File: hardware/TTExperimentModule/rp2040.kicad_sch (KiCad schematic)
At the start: 24 parts, among them J6 Conn_01x02, U5 RP2040, U6 W25Q32JVSS, Y1 12.0MHz

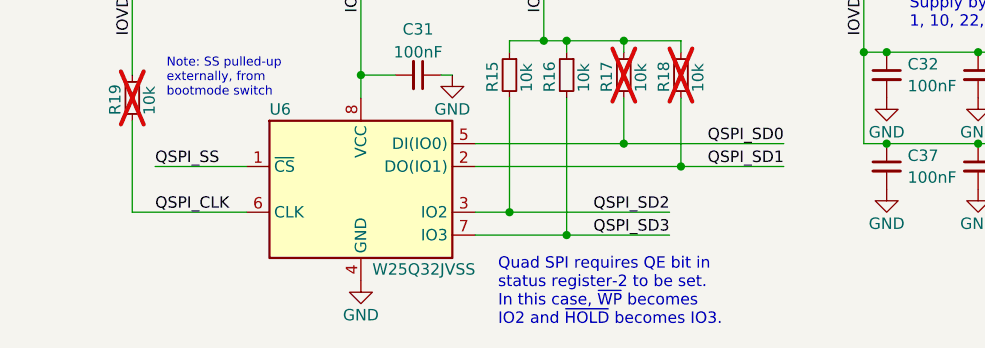
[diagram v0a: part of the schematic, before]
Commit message: reduced-height flash (dual footprint), layout rework, markings
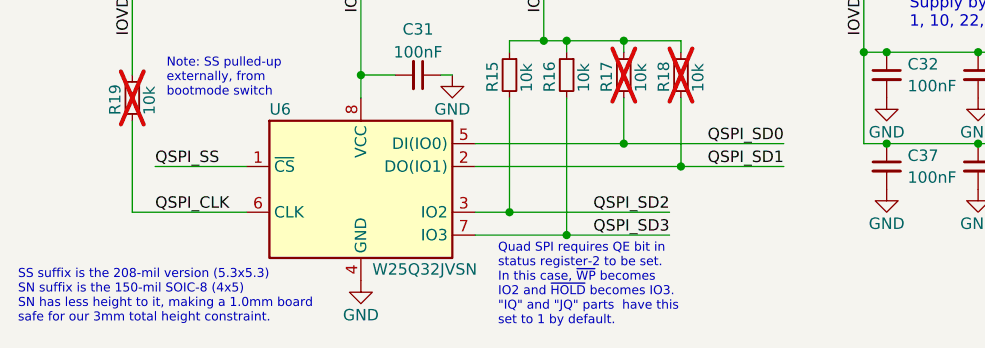
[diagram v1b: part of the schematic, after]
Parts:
- U6: value W25Q32JVSS -> W25Q32JVSN; footprint Package_SO:SOIC-8_5.3x5.3mm_P1.27mm -> Package_SO:SOIC-8_3.9x4.9mm_P1.27mm; DigikeyPN W25Q32JVSSIQ-ND -> 256-W25Q32JVSNIQTRCT-ND; LCSC C82344 -> C5355146; MPN W25Q32JVSSIQ -> W25Q32JVSNIQ TR
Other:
- note added: "Quad SPI requires QE bit in status register-2 to be set. In this case, ~{WP} becomes IO2 and ~{HOLD} becomes IO3. "IQ" and "JQ" parts have this set to 1 by default."
- note added: "SS suffix is the 208-mil version (5.3x5.3) SN suffix is the 150-mil SOIC-8 (4x5) SN has less height to it, making a 1.0mm board safe for our 3mm total height constraint."
- note removed: "Quad SPI requires QE bit in status register-2 to be set. In this case, ~{WP} becomes IO2 and ~{HOLD} becomes IO3."
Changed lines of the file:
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@@
 		)
 	)
-	(text "Quad SPI requires QE bit in \nstatus register-2 to be set.\nIn this case, ~{WP} becomes \nIO2 and ~{HOLD} becomes IO3."
+	(text "Quad SPI requires QE bit in \nstatus register-2 to be set.\nIn this case, ~{WP} becomes \nIO2 and ~{HOLD} becomes IO3.\n\"IQ\" and \"JQ\" parts  have this\nset to 1 by default."
 		(exclude_from_sim no)
 		(at 66.04 195.58 0)
 		(effects
 			(font
-				(size 1.27 1.27)
+				(size 1 1)
 			)
 			(justify left bottom)
 		)
 	)
+	(text "SS suffix is the 208-mil version (5.3x5.3)\nSN suffix is the 150-mil SOIC-8 (4x5)\nSN has less height to it, making a 1.0mm board\nsafe for our 3mm total height constraint."
+		(exclude_from_sim no)
+		(at 12.7 192.278 0)
+		(effects
+			(font
+				(size 1 1)
+			)
+			(justify left)
+		)
+	)
 	(text "Factory test\nmode: GND"
 		(exclude_from_sim no)
@@
 			"NS0wMy0yOVQyMDoxNDo0My41NjEyODNaIiBjb3VudD0iMSIvPgogICAgICAgIDwvYm9va21hcms6"
 			"YXBwbGljYXRpb25zPgogICAgICA8L21ldGFkYXRhPgogICAgPC9pbmZvPgogIDwvYm9va21hcms+"
-			"CiAgPGJvb2ttYXJrIGhyZWY9ImZpbGU6Lw=="
+			"CiAgPGJvb2ttYXJrIGhyZWY9ImZpbGU6LwBRAAAATgAAAGcAAABXAAAAawAAADUAAABlAAAAOAAA"
+			"ADEAAAB0AAAAOAAAADYAAABJAAAAUgAAAFgAAAAvAAAAVQAAAFgAAAB4AAAANgAAAHEAAABvAAAA"
+			"NgAAAEIAAAB0AAAALwAAAEcAAAAyAAAAbAAAAEIAAAAvAAAAZwAAAE0AAABPAAAARQAAAEMAAABZ"
+			"AAAANgAAADYAAAArAAAAZgAAAFEAAAA0AAAAMgAAAGkAAAB6AAAAQgAAADkAAABMAAAAbAAAAGMA"
+			"AABRAAAAMwAAADIAAAB1AAAALwAAAFkAAAB5AAAAdgAAAGYAAAA1AAAAagAAAHQAAAA4AAAAUAAA"
+			"AG8AAABWAAAARAAAAGEAAABiAAAAeAAAAGMAAABOAAAAKwAAAHgAAAAxAAAAaAAAAFUAAAB2AAAA"
+			"bAAAAE0AAABzAAAAQQAAADYAAABJAAAAMgAAAGEAAABHAAAAeQAAAFUAAABNAAAAQwAAAGIAAABB"
+			"AAAAMwAAADYAAABxAAAAcgAAAGQAAABLAAAAYwAAADkAAAByAAAANgAAAFoAAABmAAAAVwAAAGwA"
+			"AAA3AAAAWgAAAEUAAABSAAAALwAAACsAAABTAAAANwAAAFIAAABVAAAAeQAAAGYAAAAxAAAAUwAA"
+			"AFAAAAB1AAAAcwAAAEMAAABUAAAAegAAAE0AAAAxAAAAUAAAAHUAAABzAAAAMQAAAGYAAAB1AAAA"
+			"TQAAAHEAAAAxAAAATQAAAFAAAABsAAAAVwAAAFUAAAA2AAAAZgAAAC8AAABZAAAASgAAAHMAAAA3"
+			"AAAATwAAAHcAAAAxAAAAdAAAAHIAAABTAAAARQAAAHQAAABQAAAAbgAAAGgAAABWAAAAVAAAAG8A"
+			"AABHAAAAeAAAAHgAAAA4AAAAUwAAAGgAAABIAAAAQwAAAE4AAABIAAAAWAAAAHoAAABmAAAAMAAA"
+			"AFUAAABhAAAANQAAAEUAAAA1AAAAZgAAADgAAAAxAAAAagAAAFMAAABNAAAANQAAAHAAAABsAAAA"
+			"dAAAAG0AAABNAAAAagAAAGoAAABPAAAAUQAAAFcAAABzAAAAVwAAAGUAAABGAAAAcgAAAG8AAAA4"
+			"AAAAKwAAAHkAAABHAAAARAAAADIAAABiAAAAaAAAAFIAAABOAAAATwAAAHQAAAA1AAAARQAAAEsA"
+			"AAAzAAAAQgAAAGYAAAA5AAAAeQAAAEgAAABxAAAAaAAAAHYAAABiAAAAQgAAAGUAAAB3AAAAZQAA"
+			"AE4AAABGAAAAbwAAAGIAAABvAAAAdAAAAEMAAAB2AAAAVAAAAHQAAABKAAAANAAAAFYAAABBAAAA"
+			"egAAAHMAAABsAAAAdQAAAFcAAABrAAAASA=="
 		)
 	)
@@
 			)
 		)
-		(property "Value" "W25Q32JVSS"
+		(property "Value" "W25Q32JVSN"
 			(at 52.07 189.23 0)
 			(effects
@@
 			)
 		)
-		(property "Footprint" "Package_SO:SOIC-8_5.3x5.3mm_P1.27mm"
+		(property "Footprint" "Package_SO:SOIC-8_3.9x4.9mm_P1.27mm"
 			(at 50.8 180.34 0)
 			(effects
@@
 			)
 		)
-		(property "MPN" "W25Q32JVSSIQ"
+		(property "MPN" "W25Q32JVSNIQ TR"
 			(at 50.8 180.34 0)
 			(effects
@@
 			)
 		)
-		(property "DigikeyPN" "W25Q32JVSSIQ-ND"
+		(property "DigikeyPN" "256-W25Q32JVSNIQTRCT-ND"
 			(at 50.8 180.34 0)
 			(effects
@@
 			)
 		)
-		(property "LCSC" "C82344"
+		(property "LCSC" "C5355146"
 			(at 50.8 180.34 0)
 			(effects

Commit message: BOM updates for spaaaaaace
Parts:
- C27, C28: DigikeyPN (none) -> 587-3410-1-ND; LCSC C5673 -> (none); MPN CL10A105KA8NNNC -> LMK107B7105KAHT
- C29, C30: DigikeyPN (none) -> 445-13779-1-ND; LCSC C541341 -> (none); MPN CC0402BRNPO9BN6R0 -> C1005NP01H060D050BA
- C31, C32, C33, C34, C35, C36, C37, C38, C39: DigikeyPN (none) -> 490-18203-1-ND; LCSC C100072 -> (none); MPN CL05A104KA5NNNC -> GCM155L81E104KE02D
- R13, R15, R16, R17, R18, R19: DigikeyPN (none) -> 10-ERJ-H2GJ103XCT-ND; LCSC C471764 -> (none); MPN RC0402FR-0710KL -> ERJ-H2GJ103X
- R14: DigikeyPN (none) -> 10-ERJ-H2GJ102XCT-ND; LCSC C202394 -> (none); MPN CR0402-FX-1001GLF -> ERJ-H2GJ102X
